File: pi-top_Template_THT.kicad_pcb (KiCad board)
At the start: 2 copper layers, 65 x 56 mm, 6 parts, among them J1 3M 951 Series, J2 Harwin M22-655R

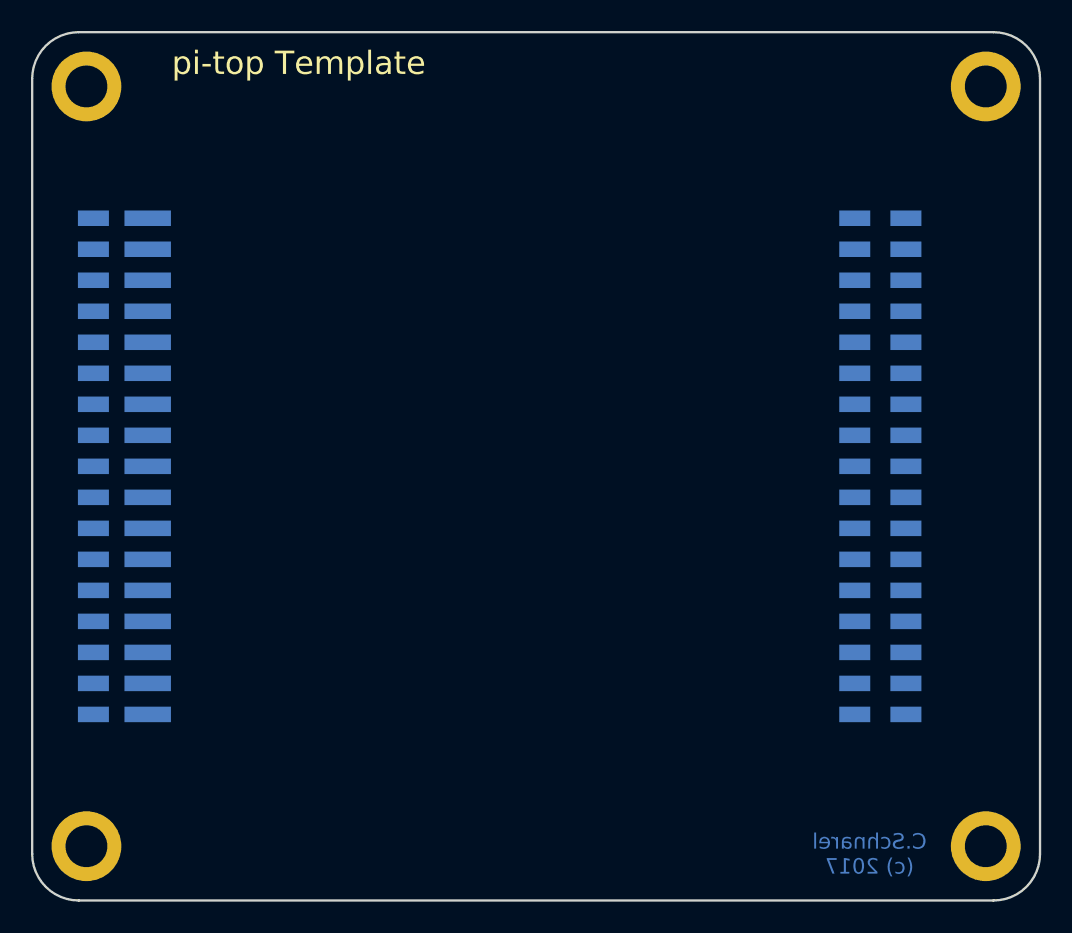
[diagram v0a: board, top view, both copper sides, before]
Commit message: Added new 3D models
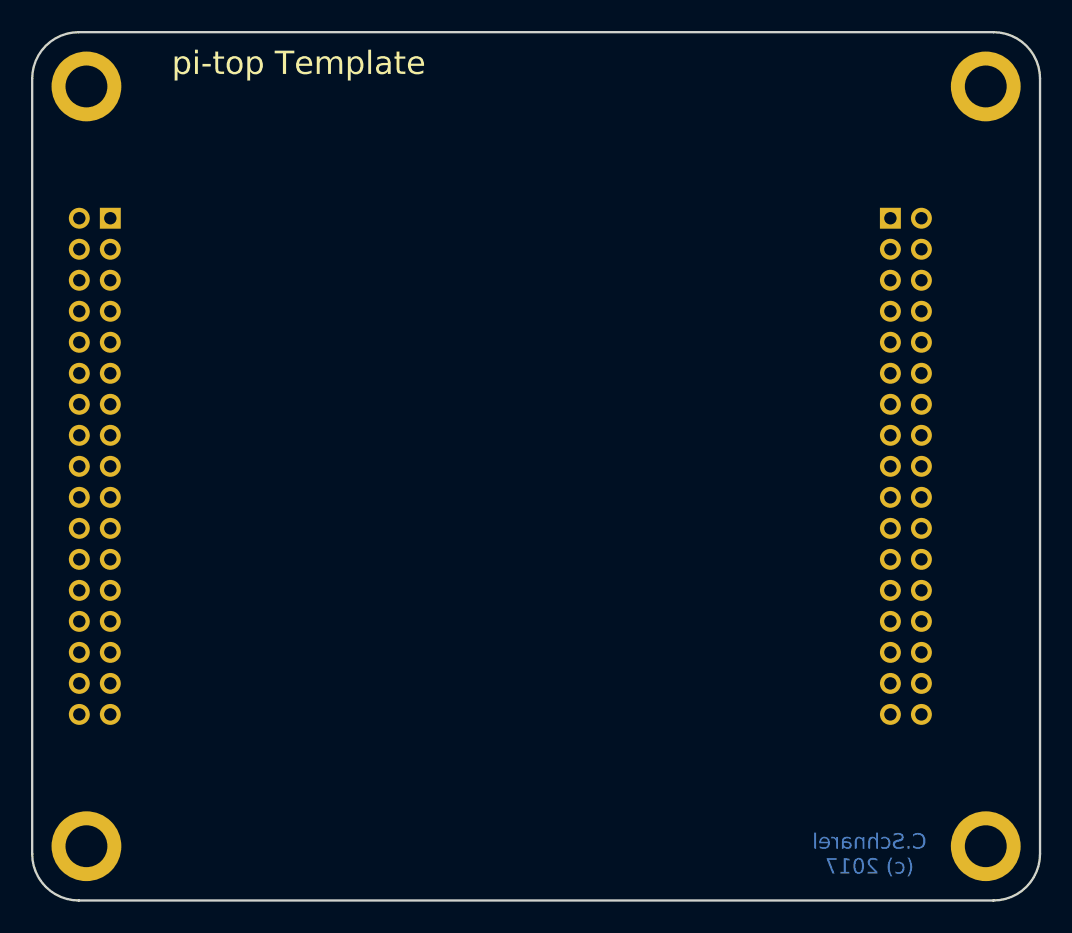
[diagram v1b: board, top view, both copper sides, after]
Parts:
- J1: footprint pi-top:3M_951217-4620-XX -> Pin_Headers:Pin_Header_Angled_2x17_Pitch2.00mm
- J2: footprint pi-top:Harwin_M22-6553442R -> Socket_Strips:Socket_Strip_Angled_2x17_Pitch2.00mm
- moved J2 16.0 mm to (93.3, 86.0), turned to 180 degrees
- moved J1 15.0 mm to (43.0, 86.0), turned to 180 degrees
